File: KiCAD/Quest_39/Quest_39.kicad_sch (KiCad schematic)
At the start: 46 parts, among them J1 1x2 Scr. Term., J10 Conn_01x05_Male, J11 1x2 Scr. Term., J12 1x2 Scr. Term, J2 1x2 Scr. Term., J3 1x2 Scr. Term., J4 1x2 Scr. Term., J5 1x2 Scr. Term., J6 1x2 Scr. Term., J7 1x2 Scr. Term., J8 1x2 Scr. Term., J9 1x2 Scr. Term., U1 AZ1117-3.3, U2 17791063215, U3 STM32F103C8T6, Y1 16MHz

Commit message: Small changes made during schematic review w/ Joost
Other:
- note added: "TODO: - Give INA's individual I2C addresses! - PWR_FLAGs to POS_x en NEG_x if necessary - Andere waarde digipot selecteren? - STM32 debug led - Copy buck design to all - LTM4611EV pins naar buiten brengen - STM32 pins naar buiten brengen"
- note removed: "TODO: - Give INA's individual I2C addresses! - PWR_FLAGs to POS_x en NEG_x if necessary"
- moved on the sheet: R3
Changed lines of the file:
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@@
-    (stroke (width 0) (type default) (color 0 0 0 0))
-  )
-  (wire (pts (xy 123.19 54.61) (xy 148.59 54.61))
     (stroke (width 0) (type default) (color 0 0 0 0))
   )
@@
     (stroke (width 0) (type default) (color 0 0 0 0))
   )
-  (wire (pts (xy 123.19 63.5) (xy 123.19 62.23))
+  (wire (pts (xy 123.19 64.77) (xy 123.19 63.5))
     (stroke (width 0) (type default) (color 0 0 0 0))
   )
@@
     (stroke (width 0) (type default) (color 0 0 0 0))
   )
+  (wire (pts (xy 148.59 54.61) (xy 123.19 54.61))
+    (stroke (width 0) (type default) (color 0 0 0 0))
+  )
   (polyline (pts (xy 107.95 96.52) (xy 111.76 96.52))
     (stroke (width 0) (type default) (color 0 0 0 0))
@@
     (stroke (width 0) (type default) (color 0 0 0 0))
   )
-  (wire (pts (xy 92.71 138.43) (xy 110.49 138.43))
+  (wire (pts (xy 92.71 138.43) (xy 118.11 138.43))
     (stroke (width 0) (type default) (color 0 0 0 0))
   )
@@
     (stroke (width 0) (type default) (color 0 0 0 0))
   )
-  (wire (pts (xy 104.14 146.05) (xy 110.49 146.05))
+  (wire (pts (xy 104.14 146.05) (xy 118.11 146.05))
     (stroke (width 0) (type default) (color 0 0 0 0))
   )
@@
   )
   (wire (pts (xy 30.48 120.65) (xy 34.29 120.65))
+    (stroke (width 0) (type default) (color 0 0 0 0))
+  )
+  (wire (pts (xy 123.19 54.61) (xy 123.19 55.88))
     (stroke (width 0) (type default) (color 0 0 0 0))
   )
@@
     (effects (font (size 2.54 2.54) (thickness 0.254) bold) (justify left bottom))
   )
-  (text "TODO:\n - Give INA's individual I2C addresses!\n - PWR_FLAGs to POS_x en NEG_x if necessary\n"
+  (text "TODO:\n - Give INA's individual I2C addresses!\n - PWR_FLAGs to POS_x en NEG_x if necessary\n - Andere waarde digipot selecteren?\n - STM32 debug led\n - Copy buck design to all\n - LTM4611EV pins naar buiten brengen\n - STM32 pins naar buiten brengen"
     (at 13.97 281.94 0)
     (effects (font (size 6 6)) (justify left bottom))
@@
     (effects (font (size 1.27 1.27)) (justify left bottom))
   )
-  (label "HSE_OUT" (at 140.97 62.23 0)
+  (label "HSE_OUT" (at 139.7 62.23 0)
     (effects (font (size 1.27 1.27)) (justify left bottom))
   )
@@
     (effects (font (size 1.27 1.27)) (justify right bottom))
   )
+  (label "HSE_IN" (at 118.11 138.43 180)
+    (effects (font (size 1.27 1.27)) (justify right bottom))
+  )
   (label "SCL" (at 58.42 67.31 180)
     (effects (font (size 1.27 1.27)) (justify right bottom))
@@
     (effects (font (size 1.27 1.27)) (justify right bottom))
   )
-  (label "HSE_IN" (at 142.24 59.69 0)
+  (label "HSE_IN" (at 139.7 59.69 0)
     (effects (font (size 1.27 1.27)) (justify left bottom))
   )
@@
     (effects (font (size 1.27 1.27)) (justify left bottom))
   )
+  (label "HSE_OUT" (at 118.11 146.05 180)
+    (effects (font (size 1.27 1.27)) (justify right bottom))
+  )
   (label "SCL" (at 107.95 92.71 0)
     (effects (font (size 1.27 1.27)) (justify left bottom))
@@
   (label "SCK" (at 58.42 33.02 180)
     (effects (font (size 1.27 1.27)) (justify right bottom))
-  )
-  (global_label "HSE_IN" (shape input) (at 110.49 138.43 0) (fields_autoplaced)
-    (effects (font (size 1.27 1.27)) (justify left))
-    (property "Intersheet References" "${INTERSHEET_REFS}" (id 0) (at 119.495 138.3506 0)
-      (effects (font (size 1.27 1.27)) (justify left) hide)
-    )
-  )
-  (global_label "HSE_OUT" (shape input) (at 139.7 62.23 180) (fields_autoplaced)
-    (effects (font (size 1.27 1.27)) (justify right))
-    (property "Intersheet References" "${INTERSHEET_REFS}" (id 0) (at 129.0017 62.1506 0)
-      (effects (font (size 1.27 1.27)) (justify right) hide)
-    )
-  )
-  (global_label "HSE_IN" (shape input) (at 139.7 59.69 180) (fields_autoplaced)
-    (effects (font (size 1.27 1.27)) (justify right))
-    (property "Intersheet References" "${INTERSHEET_REFS}" (id 0) (at 130.695 59.6106 0)
-      (effects (font (size 1.27 1.27)) (justify right) hide)
-    )
-  )
-  (global_label "HSE_OUT" (shape input) (at 110.49 146.05 0) (fields_autoplaced)
-    (effects (font (size 1.27 1.27)) (justify left))
-    (property "Intersheet References" "${INTERSHEET_REFS}" (id 0) (at 121.1883 145.9706 0)
-      (effects (font (size 1.27 1.27)) (justify left) hide)
-    )
   )
   (symbol (lib_id "power:+3.3V") (at 204.47 105.41 0) (unit 1)
@@
     (pin "2")
   )
-  (symbol (lib_id "Device:R") (at 123.19 58.42 180) (unit 1)
-    (in_bom yes) (on_board yes)
-    (property "Reference" "R3" (id 0) (at 127 57.15 0))
-    (property "Value" "10k" (id 1) (at 127 59.69 0))
-    (property "Footprint" "" (id 2) (at 124.968 58.42 90)
-      (effects (font (size 1.27 1.27)) hide)
-    )
-    (property "Datasheet" "~" (id 3) (at 123.19 58.42 0)
+  (symbol (lib_id "Device:R") (at 123.19 59.69 180) (unit 1)
+    (in_bom yes) (on_board yes)
+    (property "Reference" "R3" (id 0) (at 127 58.42 0))
+    (property "Value" "10k" (id 1) (at 127 60.96 0))
+    (property "Footprint" "" (id 2) (at 124.968 59.69 90)
+      (effects (font (size 1.27 1.27)) hide)
+    )
+    (property "Datasheet" "~" (id 3) (at 123.19 59.69 0)
       (effects (font (size 1.27 1.27)) hide)
     )
@@
     )
   )
-  (symbol (lib_id "power:GND") (at 123.19 63.5 0) (unit 1)
-    (in_bom yes) (on_board yes) (fields_autoplaced)
-    (property "Reference" "#PWR0108" (id 0) (at 123.19 69.85 0)
-      (effects (font (size 1.27 1.27)) hide)
-    )
-    (property "Value" "GND" (id 1) (at 123.19 68.58 0))
-    (property "Footprint" "" (id 2) (at 123.19 63.5 0)
-      (effects (font (size 1.27 1.27)) hide)
-    )
-    (property "Datasheet" "" (id 3) (at 123.19 63.5 0)
-      (effects (font (size 1.27 1.27)) hide)
-    )
+  (symbol (lib_id "power:GND") (at 123.19 64.77 0) (unit 1)
+    (in_bom yes) (on_board yes) (fields_autoplaced)
+    (property "Reference" "#PWR0108" (id 0) (at 123.19 71.12 0)
+      (effects (font (size 1.27 1.27)) hide)
+    )
+    (property "Value" "GND" (id 1) (at 123.19 69.85 0))
+    (property "Footprint" "" (id 2) (at 123.19 64.77 0)
+      (effects (font (size 1.27 1.27)) hide)
+    )
+    (property "Datasheet" "" (id 3) (at 123.19 64.77 0)
+      (effects (font (size 1.27 1.27)) hide)
+    )

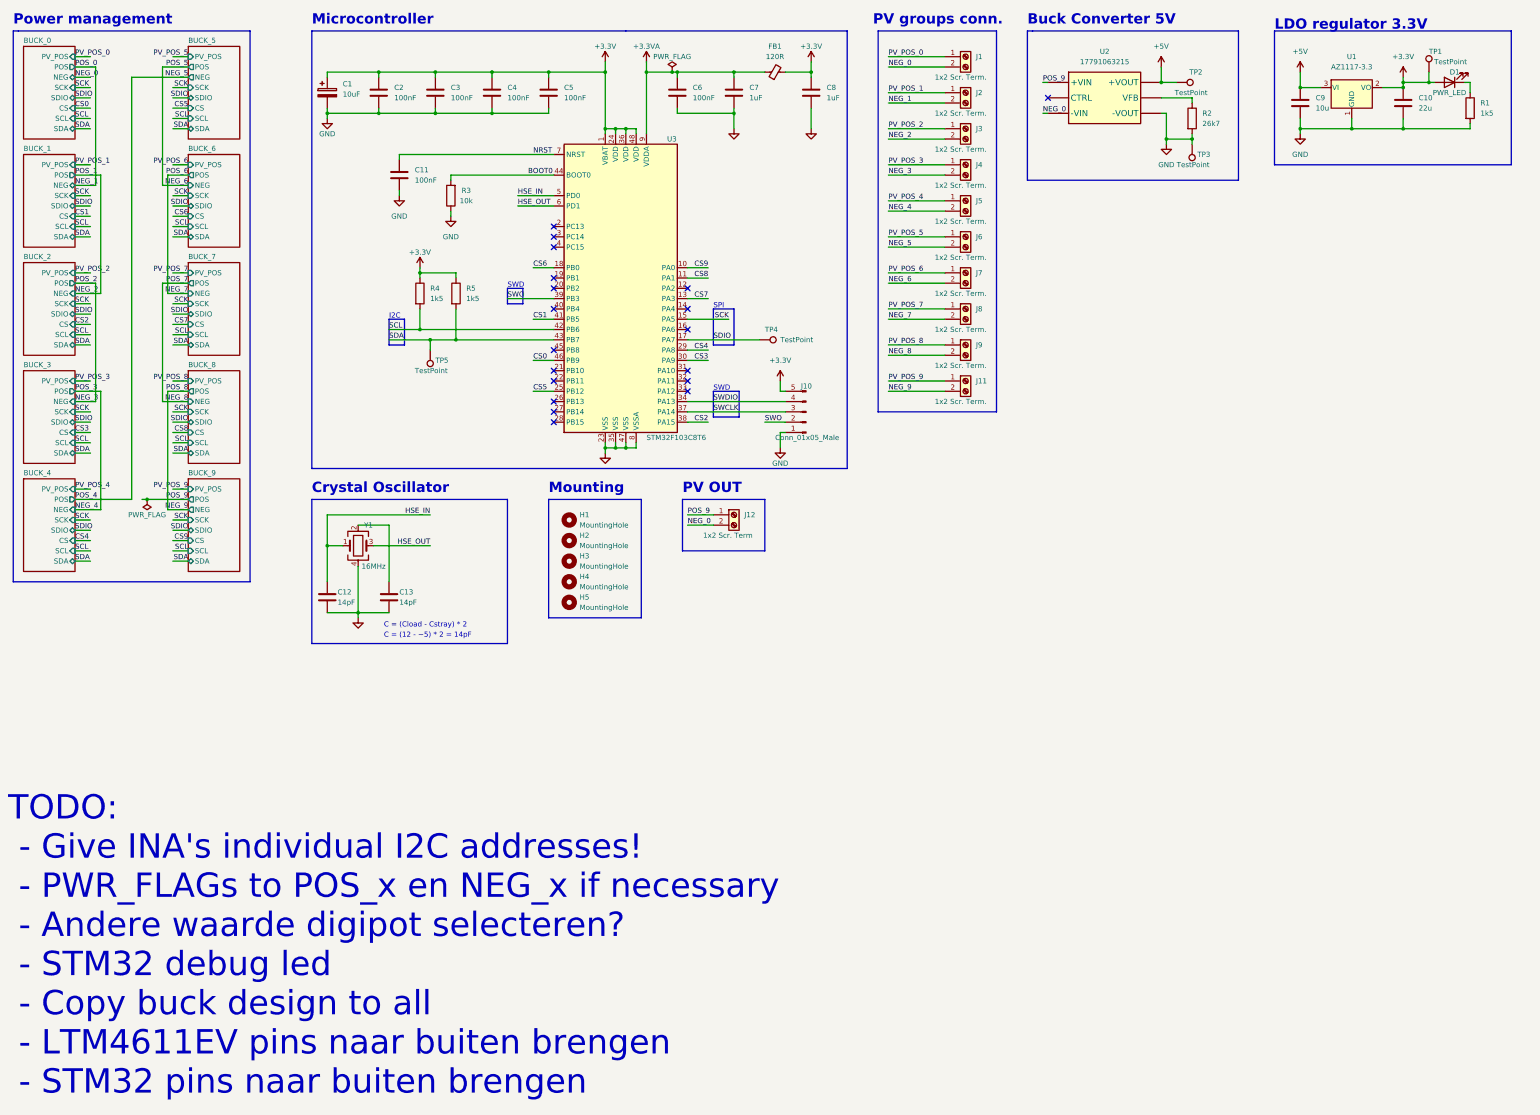
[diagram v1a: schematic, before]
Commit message: Added weak SPI CS pullups to prevent spurious behaviour
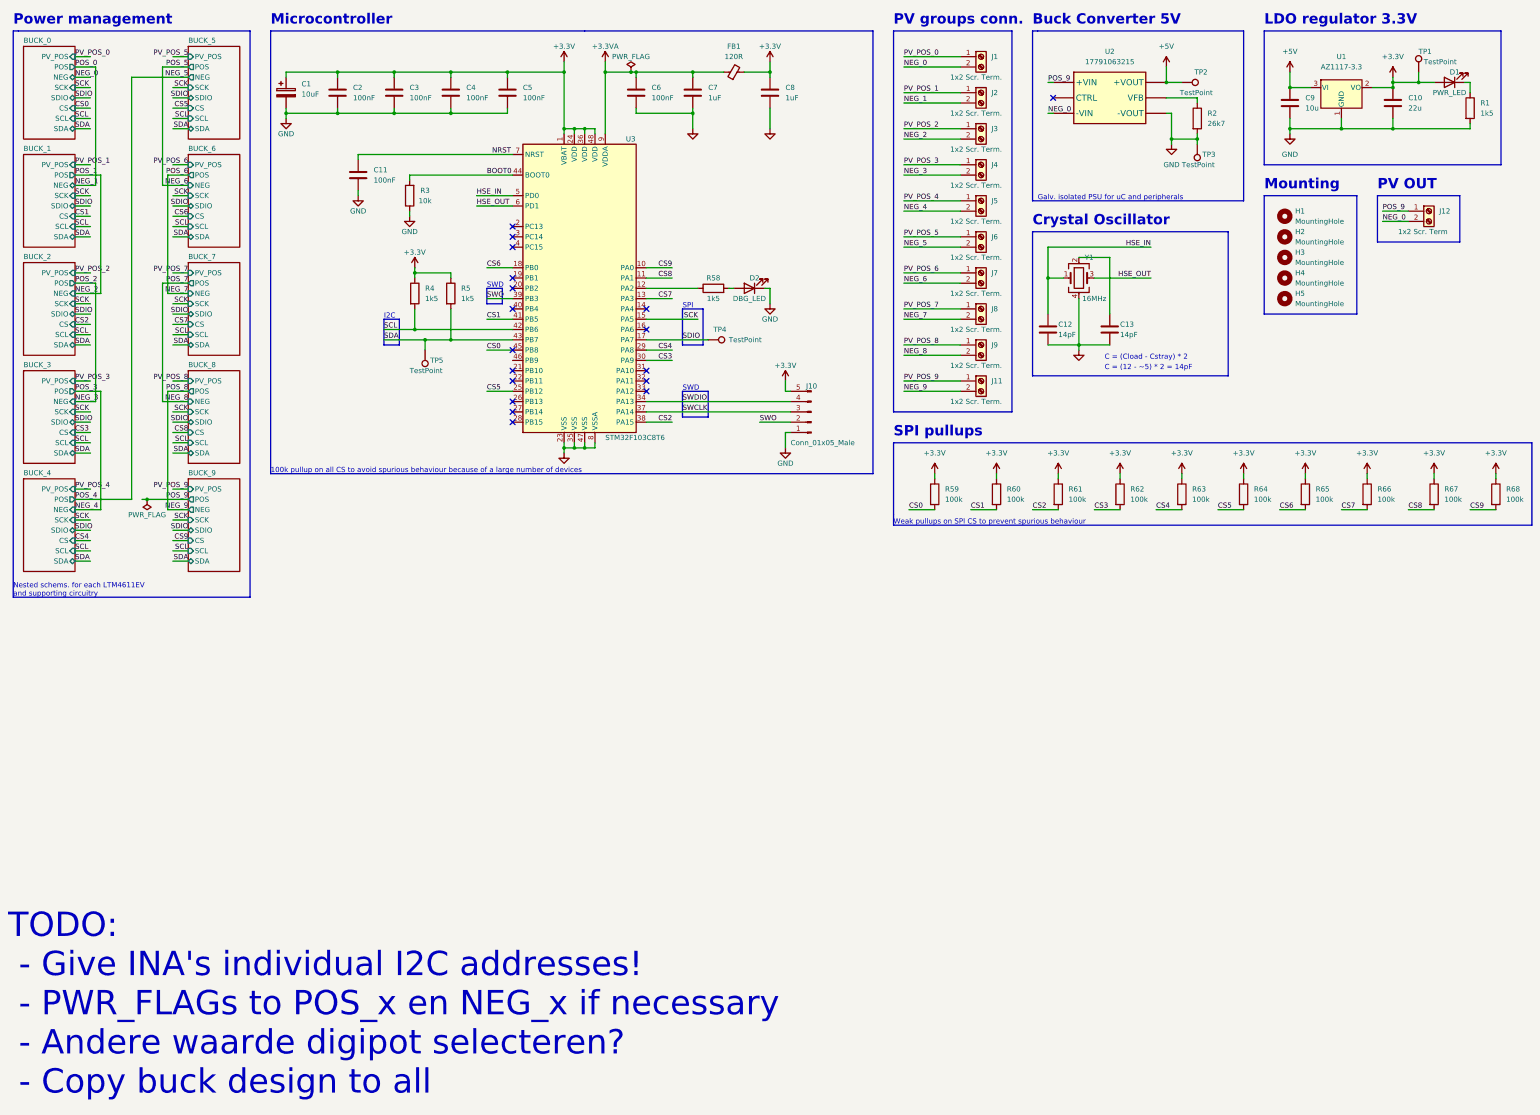
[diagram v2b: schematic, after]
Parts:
- added D2: DBG_LED, symbol Device:LED
- added R58: 1k5, symbol Device:R
- added R59, R60, R61, R62, R63, R64, R65, R66, R67, R68: 100k, symbol Device:R
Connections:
- net +3.3V: now also R59.1, R60.1, R61.1, R62.1, R63.1, R64.1, R65.1, R66.1, R67.1, R68.1
- net CS0: now also U3.45 (PB8), R59.2; no longer U3.46 (PB9)
- net CS1: now also R60.2
- net CS2: now also R61.2
- net CS3: now also R62.2
- net CS4: now also R63.2
- net CS5: now also R64.2
- net CS6: now also R65.2
- net CS7: now also R66.2
- net CS8: now also R67.2
- net CS9: now also R68.2
- net GND: now also D2.1 (K)
- net at U3.12 (PA2): now also R58.1
- new net: D2.2 (A), R58.2
- no-connect marks 19 -> 18
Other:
- note added: "100k pullup on all CS to avoid spurious behaviour because of a large number of devices"
- note added: "Galv. isolated PSU for uC and peripherals"
- note added: "Nested schems. for each LTM4611EV and supporting circuitry"
- note added: "SPI pullups"
- note added: "TODO: - Give INA's individual I2C addresses! - PWR_FLAGs to POS_x en NEG_x if necessary - Andere waarde digipot selecteren? - Copy buck design to all"
- note added: "Weak pullups on SPI CS to prevent spurious behaviour"
- note removed: "TODO: - Give INA's individual I2C addresses! - PWR_FLAGs to POS_x en NEG_x if necessary - Andere waarde digipot selecteren? - STM32 debug led - Copy buck design to all - LTM4611EV pins naar buiten brengen - STM32 pins naar buiten brengen"
- moved on the sheet: C1, C10, C11, C12, C13, C2, C3, C4, C5, C6, C7, C8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

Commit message: Gave all INA226's unique addresses
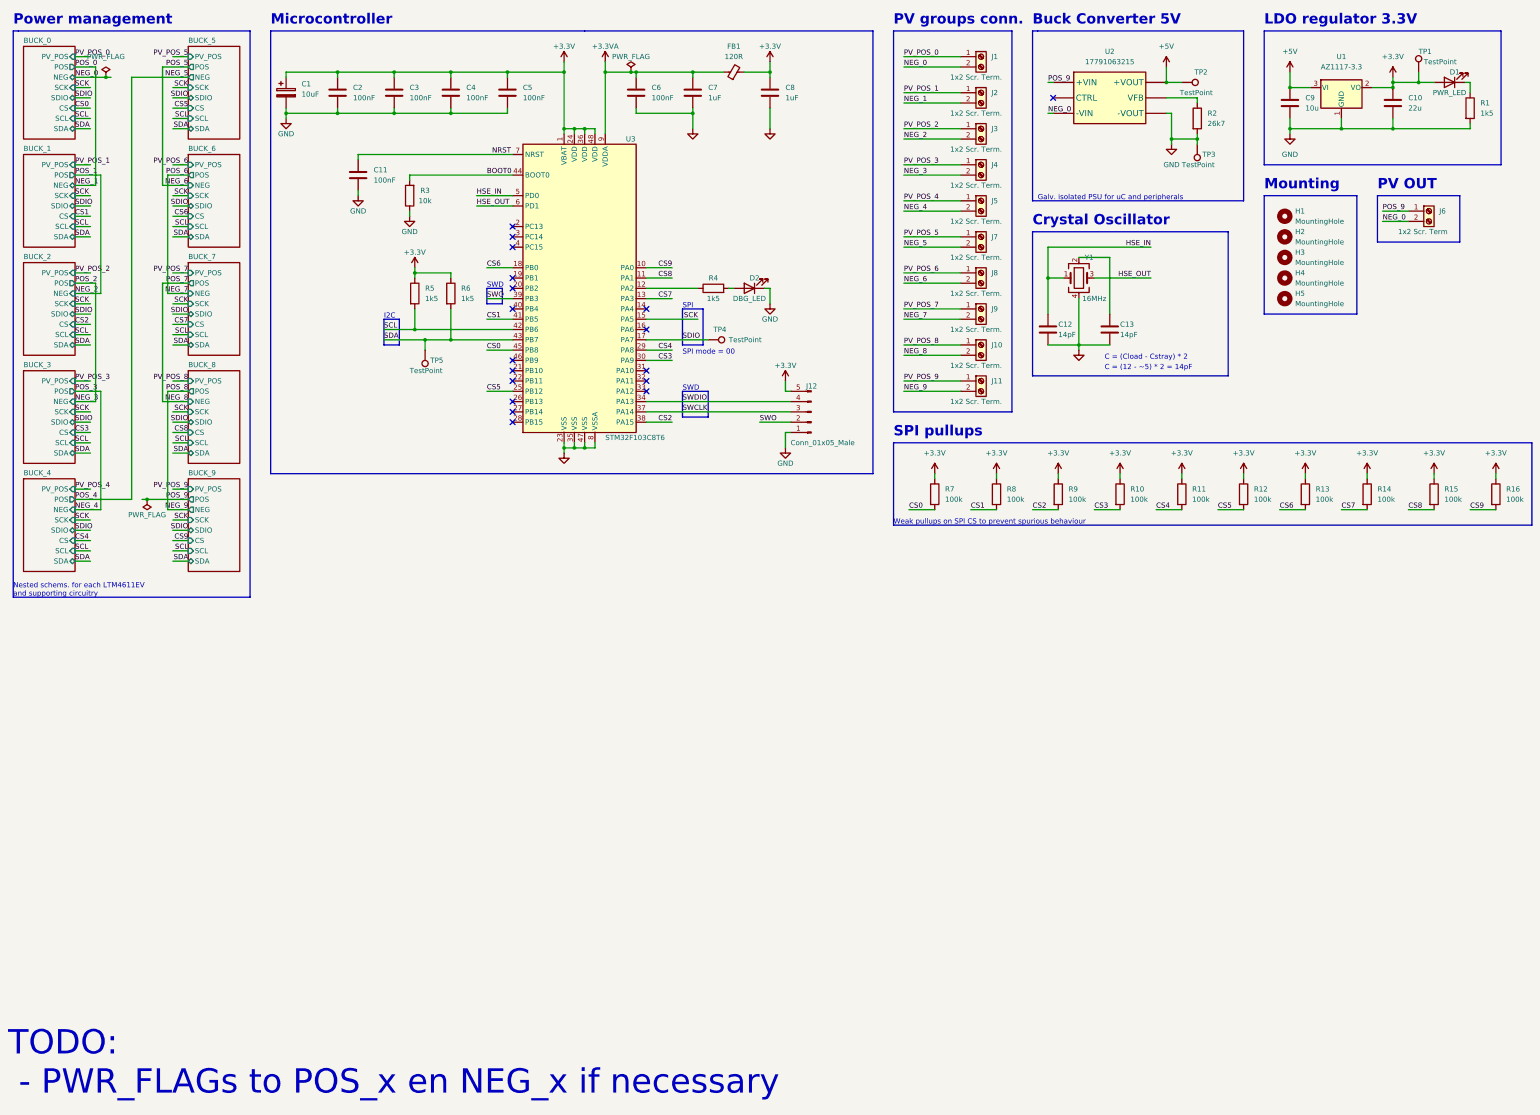
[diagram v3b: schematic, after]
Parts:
- renumbered J9 to J10, J10 to J12, J12 to J6, J6 to J7, J7 to J8, J8 to J9, R62 to R10, R63 to R11, R64 to R12, R65 to R13, R66 to R14, R67 to R15, R68 to R16, R58 to R4, R4 to R5, R5 to R6, R59 to R7, R60 to R8, R61 to R9
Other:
- note added: "SPI mode = 00"
- note added: "TODO: - PWR_FLAGs to POS_x en NEG_x if necessary"
- note removed: "100k pullup on all CS to avoid spurious behaviour because of a large number of devices"
- note removed: "TODO: - Give INA's individual I2C addresses! - PWR_FLAGs to POS_x en NEG_x if necessary - Andere waarde digipot selecteren? - Copy buck design to all"
